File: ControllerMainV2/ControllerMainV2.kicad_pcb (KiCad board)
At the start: 2 copper layers, 340 x 61.8 mm, 175 parts, among them IC1 1462039-4, IC17 TMUX6112PWR, IC18 TMUX6112PWR, IC19 TMUX6112PWR, IC2 TXU0104PWR, IC20 TMUX6112PWR, IC21 TMUX6112PWR, IC22 1462039-4, IC23 1462039-4, IC24 1462039-4, IC25 1462039-4, IC27 1462039-4, IC3 AD75019JPZ, J1 Conn_01x06, J2 Conn_01x10, J3 Conn_02x08_Odd_Even, J4 Conn_02x08_Odd_Even, Q1 2N7002, Q2 2N7002, Q3 2N7002, Q4 2N7002, Q5 2N7002, Q6 2N7002, Q7 EL817S1_A__TU_-F, T1 Lehle_MZ_P, U1 MCP23009-E_SO, U10 TL072, U12 TL072, U13 TL072, U14 MCP23009-E_SO, U15 MCP23009-E_SO, U16 MCP23009-E_SO, U18 TL074, U2 MCP23009-E_SO, U9 TL074

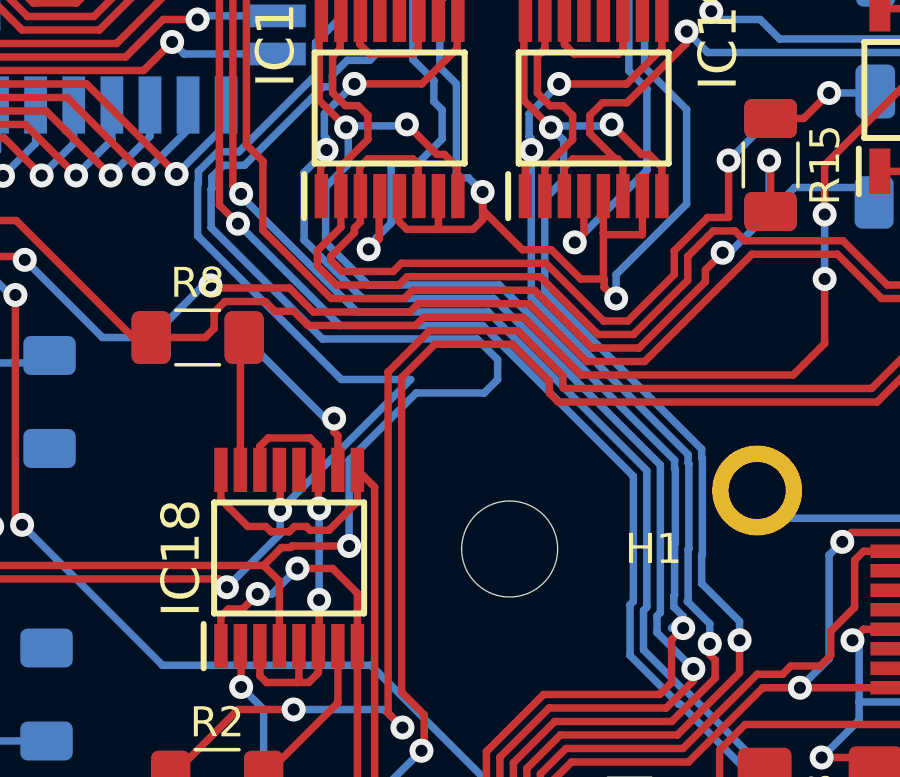
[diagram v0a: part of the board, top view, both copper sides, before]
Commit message: Changed Enclosure bottom for 8 loops
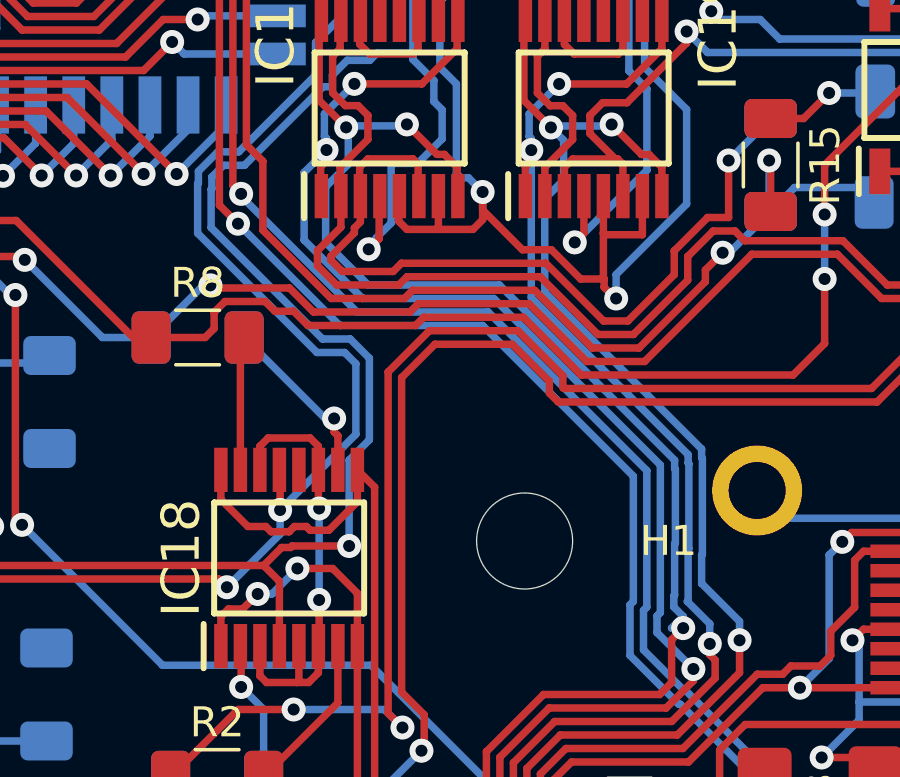
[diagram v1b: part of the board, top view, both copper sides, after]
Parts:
- moved H1 0.57 mm to (351.3, 161.9)
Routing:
- net /VSS_15V0: track 631.0 -> 623.7 mm
- net /VDD_15V0: track 622.1 -> 619.7 mm

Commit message: Enclosure and faceplate for 8 loops
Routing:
- net /out2: track 225.0 -> 220.1 mm
- net /CS: track 94.1 -> 91.0 mm
- net /SwitchMatrix/VDD5V0_i: track 79.8 -> 77.4 mm
- net /RCLK: track 74.6 -> 72.8 mm
- net /MOSI: track 69.9 -> 68.1 mm
- net /SCLK: track 66.5 -> 64.8 mm
- net /VDD_3V3: track 572.7 -> 571.0 mm
- net /SDA: track 389.9 -> 390.8 mm
- net /VSS_15V0: track 623.7 -> 622.9 mm
- net /INT: track 404.7 -> 404.1 mm

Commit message: Layout of PGAs
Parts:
- added C27: 22n, Capacitor_SMD:C_1206_3216Metric_Pad1.33x1.80mm_HandSolder, F.Cu at (116.8, 136.0)
- added C28: 22n, Capacitor_SMD:C_1206_3216Metric_Pad1.33x1.80mm_HandSolder, F.Cu at (116.8, 130.6)
- added C29: 1u, Capacitor_SMD:C_1206_3216Metric_Pad1.33x1.80mm_HandSolder, B.Cu at (150.2, 136.8)
- added C32: 1u, Capacitor_SMD:C_1206_3216Metric_Pad1.33x1.80mm_HandSolder, B.Cu at (150.0, 130.3)
- added C33: 1u, Capacitor_SMD:C_1206_3216Metric_Pad1.33x1.80mm_HandSolder, F.Cu at (122.8, 130.6)
- added C34: 1u, Capacitor_SMD:C_1206_3216Metric_Pad1.33x1.80mm_HandSolder, F.Cu at (122.8, 136.0)
- added C35: 100n, Capacitor_SMD:C_1206_3216Metric_Pad1.33x1.80mm_HandSolder, B.Cu at (140.9, 136.3)
- added C36: 100n, Capacitor_SMD:C_1206_3216Metric_Pad1.33x1.80mm_HandSolder, B.Cu at (140.9, 131.3)
- added C39: 100n, Capacitor_SMD:C_1206_3216Metric_Pad1.33x1.80mm_HandSolder, B.Cu at (154.2, 129.3)
- added C40: 100n, Capacitor_SMD:C_1206_3216Metric_Pad1.33x1.80mm_HandSolder, B.Cu at (145.9, 136.4)
- added IC4: AD5293BRUZ-20-RL7, SamacSys_Parts:SOP65P640X120-14N, F.Cu at (152.8, 136.6)
- added IC5: AD5293BRUZ-20-RL7, SamacSys_Parts:SOP65P640X120-14N, F.Cu at (152.8, 129.8)
- added R71: 2.2M, Resistor_SMD:R_1206_3216Metric_Pad1.30x1.75mm_HandSolder, B.Cu at (110.6, 136.0)
- added R72: 2.2M, Resistor_SMD:R_1206_3216Metric_Pad1.30x1.75mm_HandSolder, B.Cu at (110.6, 130.6)
- added R73: 2.2M, Resistor_SMD:R_1206_3216Metric_Pad1.30x1.75mm_HandSolder, B.Cu at (116.8, 136.0)
- added R74: 2.2M, Resistor_SMD:R_1206_3216Metric_Pad1.30x1.75mm_HandSolder, B.Cu at (116.8, 130.6)
- added R75: 2.2k, Resistor_SMD:R_1206_3216Metric_Pad1.30x1.75mm_HandSolder, B.Cu at (160.3, 130.4)
- added R76: 100, Resistor_SMD:R_1206_3216Metric_Pad1.30x1.75mm_HandSolder, F.Cu at (128.4, 130.6)
- added R77: 100, Resistor_SMD:R_1206_3216Metric_Pad1.30x1.75mm_HandSolder, F.Cu at (128.6, 136.0)
- added R78: 100k, Resistor_SMD:R_1206_3216Metric_Pad1.30x1.75mm_HandSolder, B.Cu at (122.8, 130.6)
- added R79: 100k, Resistor_SMD:R_1206_3216Metric_Pad1.30x1.75mm_HandSolder, B.Cu at (122.8, 135.9)
- added U3: TL074, SamacSys_Parts:SOIC127P600X175-14N, F.Cu at (136.5, 133.3)
- J1: value Conn_01x06 -> Conn_01x07; footprint Connector_JST:JST_PH_B6B-PH-K_1x06_P2.00mm_Vertical -> Connector_JST:JST_PH_B7B-PH-K_1x07_P2.00mm_Vertical
- R22, R23, R24, R25, R26, R27, R28, R29: value 4.7M -> 2.2M
- moved J1 2.00 mm to (392.0, 178.4)
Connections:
- net /SwitchMatrix/In2 renamed /amp1_out
- net /SwitchMatrix/In3 renamed /amp2_out
- net /SwitchMatrix/Out1 renamed /amp1
- net /SwitchMatrix/Out2 renamed /amp2
- J1 pad 1: /VDD_15V0 -> /CS_Amp_N
- J1 pad 2: /VSS_15V0 -> /VDD_15V0
- J1 pad 3: /VDD_3V3 -> /VSS_15V0
- J1 pad 4: /VDD_5V0 -> /VDD_3V3
- J1 pad 5: GND -> /VDD_5V0
- J1 pad 6: /I2C_Reset -> GND
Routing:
- net /CS_Amp_N: track 0.00 -> 298.5 mm, vias 0 -> 5
- net /amp2_out: track 21.4 -> 241.6 mm, vias 1 -> 4
- net /amp1_out: track 22.0 -> 237.3 mm, vias 1 -> 5
- net /SCLK: track 64.8 -> 275.0 mm, vias 1 -> 7
- net /MOSI: track 68.1 -> 271.7 mm, vias 0 -> 6
- net /I2C_Reset: track 366.6 -> 478.4 mm, vias 14 -> 23
- net /VDD_3V3: track 571.0 -> 669.0 mm, vias 14 -> 23
- net /amp2: track 171.1 -> 268.6 mm, vias 1 -> 4
- net /amp1: track 168.2 -> 261.9 mm, vias 1 -> 4
- net GND: track 613.4 -> 670.3 mm, vias 39 -> 43
- net /VDD_15V0: track 619.9 -> 676.0 mm, vias 23 -> 27
- net /VSS_15V0: track 622.9 -> 662.4 mm, vias 14 -> 18
- net Net-(IC4-Pad5): track 0.00 -> 29.0 mm, vias 0 -> 2
- net Net-(C27-Pad2): track 0.00 -> 27.4 mm, vias 0 -> 3
- net Net-(C28-Pad2): track 0.00 -> 27.0 mm, vias 0 -> 2
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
